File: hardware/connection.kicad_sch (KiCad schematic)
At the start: 9 parts, among them J6 Conn_Controller

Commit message: ✨ Further schematic updates
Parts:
- added TP7: VIN, TestPoint:TestPoint_Loop_D2.50mm_Drill1.0mm, symbol Connector:TestPoint
- added TP8: VBUS, TestPoint:TestPoint_Loop_D2.50mm_Drill1.0mm, symbol Connector:TestPoint
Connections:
- net VBUS: now also TP8.1
- net VIN: now also TP7.1
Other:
- moved on the sheet: C14, D1, F1, FL1

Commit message: 📂 PCB updates
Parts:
- removed C18, C19: 10uF/10V, symbol Device:C
- removed D1: D_TVS, symbol Device:D_TVS
- removed F1: Polyfuse, symbol Device:Polyfuse
- added F2: Fuse, Fuse:Fuse_2512_6332Metric_Pad1.52x3.35mm_HandSolder, symbol Device:Fuse
- added J3: Conn_Buttons, Connector_JST:JST_PH_S4B-PH-SM4-TB_1x04-1MP_P2.00mm_Horizontal, symbol Connector_Generic:Conn_01x04
- added R26, R27, R28, R29: 0, Resistor_SMD:R_0603_1608Metric, symbol Device:R
- added TP9: GND, TestPoint:TestPoint_Pad_D1.0mm, symbol Connector:TestPoint
- C14: footprint (none) -> Capacitor_SMD:C_0805_2012Metric
- C15, C16: footprint (none) -> Capacitor_SMD:C_1206_3216Metric
- FL1: value EMI_Filter -> ACT32P-102-2P-TL01; footprint (none) -> PEAK:ACT32P_TDK
- J6: footprint (none) -> Connector_JST:JST_PH_S5B-PH-SM4-TB_1x05-1MP_P2.00mm_Horizontal
- TP7, TP8: footprint TestPoint:TestPoint_Loop_D2.50mm_Drill1.0mm -> TestPoint:TestPoint_Pad_D1.0mm
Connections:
- net GND: now also J3.4 (Pin_4), TP9.1
- net RX/CANH: now also R26.2, R28.2
- net TX/CANL: now also R27.2, R29.2
- net at FL1.1: now also F2.2
- net VIN renamed +BATT
- net +BATT: now also F2.1
- new net Button_D: J3.3 (Pin_3)
- new net Button_P: J3.2 (Pin_2)
- new net Button_U: J3.1 (Pin_1)
- new net CANH: R28.1
- new net CANL: R29.1
- new net RX: R26.1
- new net TX: R27.1
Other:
- moved on the sheet: C15, C16

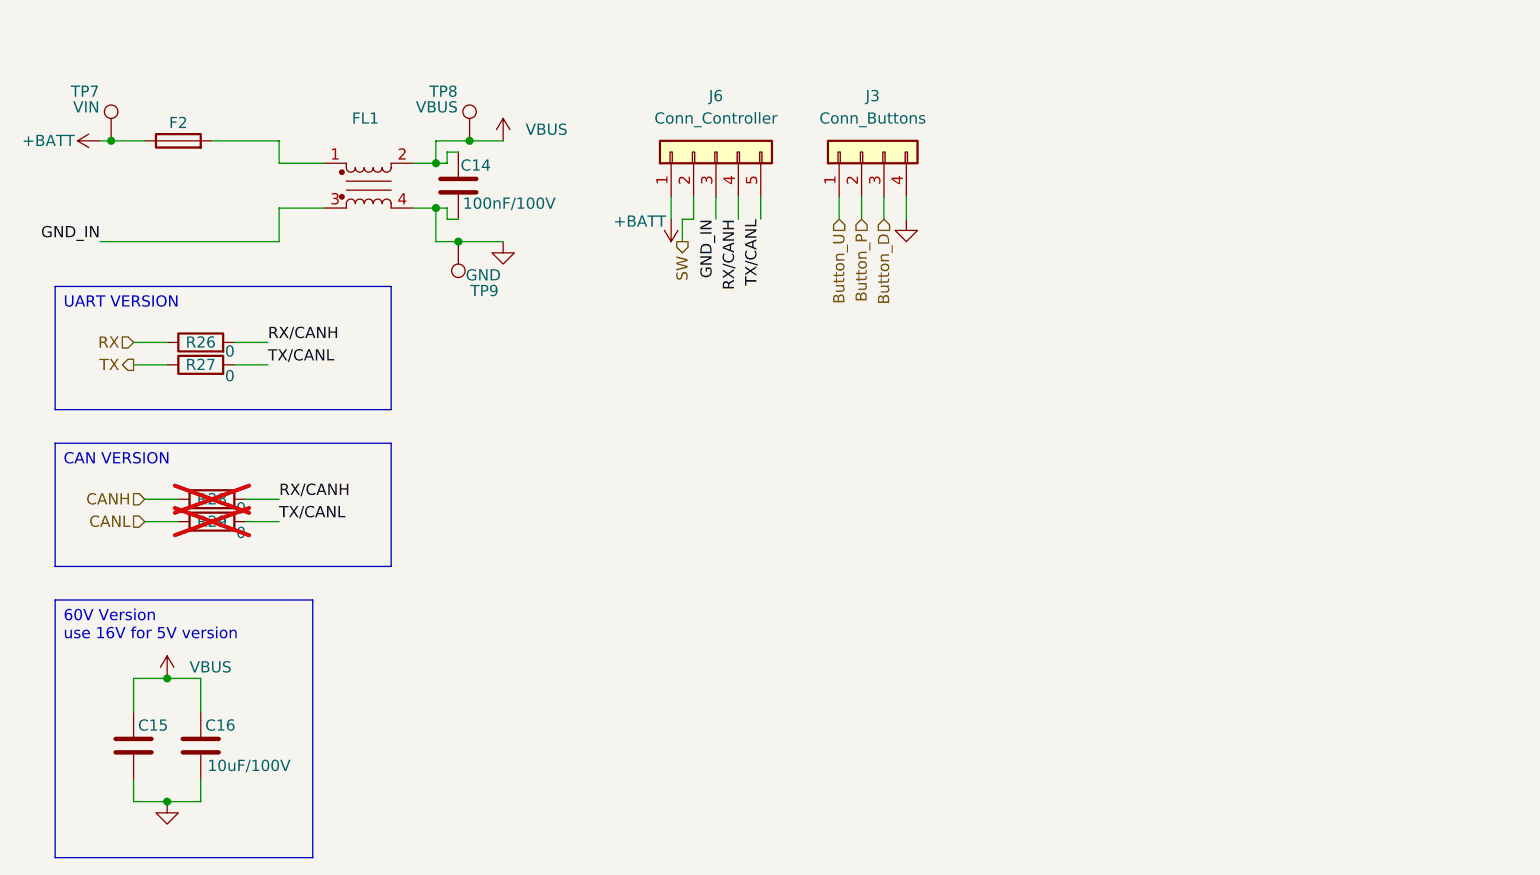
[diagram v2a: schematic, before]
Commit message: 🐛 Fix errors from rev1.0
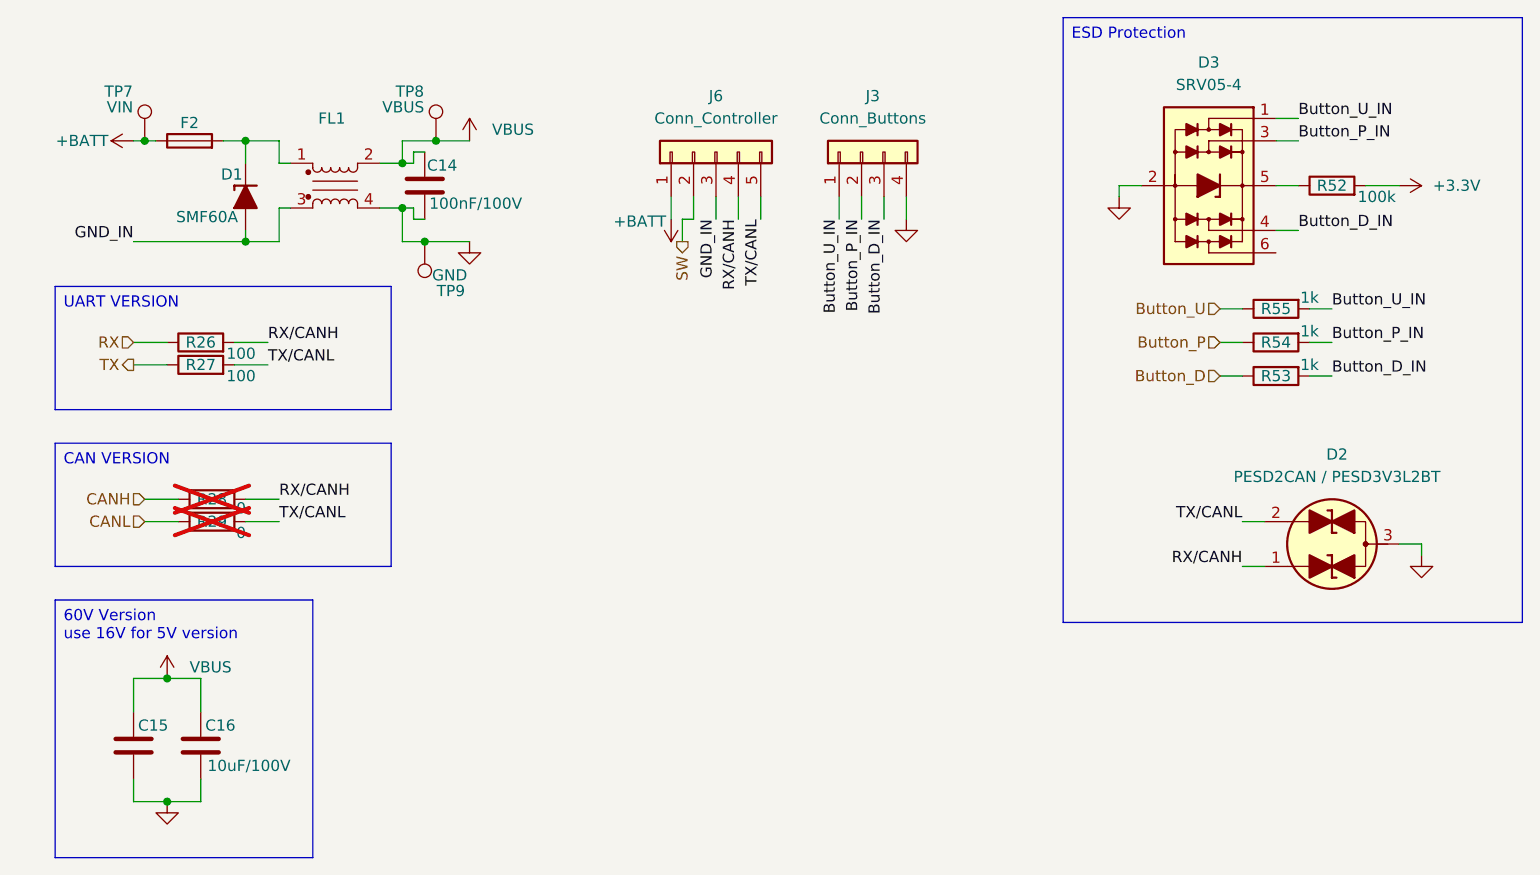
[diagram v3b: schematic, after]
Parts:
- added D1: SMF60A, Diode_SMD:D_SOD-123F, symbol PCM_Diode_TVS_AKL:D_TVS_Unidirectional_Generic
- added D2: PESD2CAN / PESD3V3L2BT, PCM_Package_TO_SOT_SMD_AKL:SOT-23, symbol PCM_Diode_TVS_AKL:PESD2CAN
- added D3: SRV05-4, PCM_Package_TO_SOT_SMD_AKL:SOT-23-6, symbol PCM_Diode_TVS_AKL:SRV05-4
- added R52: 100k, Resistor_SMD:R_0603_1608Metric, symbol Device:R
- added R53, R54, R55: 1k, Resistor_SMD:R_0603_1608Metric, symbol Device:R
- F2: footprint Fuse:Fuse_2512_6332Metric_Pad1.52x3.35mm_HandSolder -> PCM_Fuse_AKL:Fuse_1206_3216Metric
- J3: footprint Connector_JST:JST_PH_S4B-PH-SM4-TB_1x04-1MP_P2.00mm_Horizontal -> Connector_Molex:Molex_PicoBlade_53261-0471_1x04-1MP_P1.25mm_Horizontal
- J6: footprint Connector_JST:JST_PH_S5B-PH-SM4-TB_1x05-1MP_P2.00mm_Horizontal -> Connector_Molex:Molex_PicoBlade_53261-0571_1x05-1MP_P1.25mm_Horizontal
- R26, R27: value 0 -> 100
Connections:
- net Button_D: now also R53.1; no longer J3.3 (Pin_3)
- net Button_P: now also R54.1; no longer J3.2 (Pin_2)
- net Button_U: now also R55.1; no longer J3.1 (Pin_1)
- net GND: now also D2.3 (Com), D3.2 (VN)
- net GND_IN: now also D1.2 (A)
- net RX/CANH: now also D2.1 (A1)
- net TX/CANL: now also D2.2 (A2)
- net at F2.2, FL1.1: now also D1.1 (K)
- new net: D3.5 (VP), R52.1
- new net +3.3V: R52.2
- new net Button_D_IN: D3.4 (L3), J3.3 (Pin_3), R53.2
- new net Button_P_IN: D3.3 (L2), J3.2 (Pin_2), R54.2
- new net Button_U_IN: D3.1 (L1), J3.1 (Pin_1), R55.2
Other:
- moved on the sheet: C14, F2, FL1, TP7, TP8, TP9

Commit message: 🔥 Redo the PCB
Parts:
- removed FL1: ACT32P-102-2P-TL01, PEAK:ACT32P_TDK, symbol Device:Filter_EMI_LL
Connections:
- net GND_IN is gone; now on net GND: D1.2 (A), J6.3 (Pin_3)
- net VBUS: now also D1.1 (K), F2.2
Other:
- moved on the sheet: C14
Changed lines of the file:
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@@
-	)
-	(junction
-		(at 62.23 43.18)
-		(diameter 0)
-		(color 0 0 0 0)
 	)
 	(junction
@@
 	)
 	(junction
-		(at 62.23 38.1)
+		(at 57.15 46.99)
+		(diameter 0)
+		(color 0 0 0 0)
+	)
+	(junction
+		(at 57.15 35.56)
 		(diameter 0)
 		(color 0 0 0 0)
@@
 	(wire
 		(pts
+			(xy 57.15 46.99) (xy 64.77 46.99)
+		)
+		(stroke
+			(width 0)
+			(type default)
+		)
+	)
+	(wire
+		(pts
 			(xy 31.75 110.49) (xy 31.75 107.95)
 		)
@@
 	(wire
 		(pts
-			(xy 63.5 44.45) (xy 63.5 43.18)
-		)
-		(stroke
-			(width 0)
-			(type default)
-		)
-	)
-	(wire
-		(pts
-			(xy 62.23 38.1) (xy 63.5 38.1)
+			(xy 57.15 35.56) (xy 66.04 35.56)
 		)
 		(stroke
@@
 	(wire
 		(pts
-			(xy 62.23 35.56) (xy 66.04 35.56)
-		)
-		(stroke
-			(width 0)
-			(type default)
-		)
-	)
-	(wire
-		(pts
 			(xy 93.98 44.45) (xy 95.25 44.45)
 		)
@@
 	(wire
 		(pts
-			(xy 63.5 43.18) (xy 62.23 43.18)
-		)
-		(stroke
-			(width 0)
-			(type default)
-		)
-	)
-	(wire
-		(pts
 			(xy 111.76 41.91) (xy 111.76 44.45)
 		)
@@
 	(wire
 		(pts
-			(xy 62.23 46.99) (xy 64.77 46.99)
-		)
-		(stroke
-			(width 0)
-			(type default)
-		)
-	)
-	(wire
-		(pts
 			(xy 102.87 41.91) (xy 102.87 44.45)
 		)
@@
 	(wire
 		(pts
-			(xy 48.26 35.56) (xy 48.26 38.1)
-		)
-		(stroke
-			(width 0)
-			(type default)
-		)
-	)
-	(wire
-		(pts
 			(xy 41.91 35.56) (xy 44.45 35.56)
 		)
@@
 	(wire
 		(pts
-			(xy 44.45 46.99) (xy 48.26 46.99)
+			(xy 44.45 46.99) (xy 57.15 46.99)
 		)
 		(stroke
@@
 	(wire
 		(pts
-			(xy 62.23 43.18) (xy 62.23 46.99)
-		)
-		(stroke
-			(width 0)
-			(type default)
-		)
-	)
-	(wire
-		(pts
 			(xy 39.37 107.95) (xy 39.37 110.49)
 		)
@@
 	(wire
 		(pts
+			(xy 57.15 44.45) (xy 57.15 46.99)
+		)
+		(stroke
+			(width 0)
+			(type default)
+		)
+	)
+	(wire
+		(pts
 			(xy 143.51 41.91) (xy 143.51 40.64)
 		)
@@
 	(wire
 		(pts
-			(xy 62.23 38.1) (xy 62.23 35.56)
-		)
-		(stroke
-			(width 0)
-			(type default)
-		)
-	)
-	(wire
-		(pts
 			(xy 171.45 40.64) (xy 175.26 40.64)
 		)
@@
 	(wire
 		(pts
-			(xy 59.69 43.18) (xy 62.23 43.18)
-		)
-		(stroke
-			(width 0)
-			(type default)
-		)
-	)
-	(wire
-		(pts
-			(xy 64.77 36.83) (xy 63.5 36.83)
-		)
-		(stroke
-			(width 0)
-			(type default)
-		)
-	)
-	(wire
-		(pts
 			(xy 43.18 58.42) (xy 46.99 58.42)
 		)
@@
 	(wire
 		(pts
+			(xy 57.15 35.56) (xy 57.15 36.83)
+		)
+		(stroke
+			(width 0)
+			(type default)
+		)
+	)
+	(wire
+		(pts
 			(xy 39.37 100.33) (xy 39.37 96.52)
 		)
@@
 	(wire
 		(pts
-			(xy 63.5 36.83) (xy 63.5 38.1)
-		)
-		(stroke
-			(width 0)
-			(type default)
-		)
-	)
-	(wire
-		(pts
-			(xy 48.26 38.1) (xy 49.53 38.1)
-		)
-		(stroke
-			(width 0)
-			(type default)
-		)
-	)
-	(wire
-		(pts
-			(xy 49.53 43.18) (xy 48.26 43.18)
-		)
-		(stroke
-			(width 0)
-			(type default)
-		)
-	)
-	(wire
-		(pts
 			(xy 93.98 44.45) (xy 93.98 46.99)
 		)
@@
 	(wire
 		(pts
-			(xy 59.69 38.1) (xy 62.23 38.1)
-		)
-		(stroke
-			(width 0)
-			(type default)
-		)
-	)
-	(wire
-		(pts
-			(xy 64.77 44.45) (xy 63.5 44.45)
-		)
-		(stroke
-			(width 0)
-			(type default)
-		)
-	)
-	(wire
-		(pts
 			(xy 119.38 41.91) (xy 119.38 44.45)
 		)
@@
 	(wire
 		(pts
-			(xy 48.26 43.18) (xy 48.26 46.99)
-		)
-		(stroke
-			(width 0)
-			(type default)
-		)
-	)
-	(wire
-		(pts
-			(xy 44.45 35.56) (xy 48.26 35.56)
+			(xy 44.45 35.56) (xy 57.15 35.56)
 		)
 		(stroke
@@
 	(symbol
 		(lib_id "Device:C")
-		(at 64.77 40.64 0)
+		(at 57.15 40.64 0)
 		(unit 1)
 		(exclude_from_sim no)
@@
 		(dnp no)
 		(property "Reference" "C14"
-			(at 65.024 38.354 0)
+			(at 57.404 38.354 0)
 			(effects
 				(font
@@
 		)
 		(property "Value" "100nF/100V"
-			(at 65.278 42.672 0)
+			(at 57.658 42.672 0)
 			(effects
 				(font
@@
 		)
 		(property "Footprint" "Capacitor_SMD:C_0805_2012Metric"
-			(at 65.7352 44.45 0)
+			(at 58.1152 44.45 0)
 			(effects
 				(font
@@
 		)
 		(property "Datasheet" "~"
-			(at 64.77 40.64 0)
+			(at 57.15 40.64 0)
 			(effects
 				(font
@@
 		)
 		(property "Description" "Unpolarized capacitor"
-			(at 64.77 40.64 0)
+			(at 57.15 40.64 0)
 			(effects
 				(font
@@
 					(unit 1)
 				)
-			)
-		)
-	)
-	(symbol
-		(lib_id "Device:Filter_EMI_LL")
-		(at 54.61 40.64 0)
-		(unit 1)
-		(exclude_from_sim no)
-		(in_bom yes)
-		(on_board yes)
-		(dnp no)
-		(fields_autoplaced yes)
-		(property "Reference" "FL1"
-			(at 54.229 33.02 0)
-			(effects
-				(font
-					(size 1.27 1.27)
-				)
-			)
-		)
-		(property "Value" "ACT32P-102-2P-TL01"
-			(at 54.229 35.56 0)
-			(effects
-				(font
-					(size 1.27 1.27)
-				)
-				(hide yes)
-			)
-		)
-		(property "Footprint" "PEAK:ACT32P_TDK"
-			(at 54.61 39.624 0)
-			(effects
-				(font
-					(size 1.27 1.27)
-				)
-				(hide yes)
-			)
-		)
-		(property "Datasheet" "~"
-			(at 54.61 39.624 0)
-			(effects
-				(font
-					(size 1.27 1.27)
-				)
-				(hide yes)
-			)
-		)
-		(property "Description" "EMI 2-inductor filter"
-			(at 54.61 40.64 0)
-			(effects
-				(font
-					(size 1.27 1.27)
-				)
-				(hide yes)
-			)
-		)
-		(pin "1"
-		)
-		(pin "4"
-		)
-		(pin "2"
-		)
-		(pin "3"
-		)
-		(instances
-			(project ""
-				(path "/54a54a18-4a65-4728-b17a-32b4a97370c1/7b8eb5a1-fed9-4601-b83f-2313cfb612ed"
-					(reference "FL1")
-					(unit 1)
-				)
